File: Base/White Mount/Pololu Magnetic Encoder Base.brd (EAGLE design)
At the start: 26.7 x 33.7 mm, 0 parts

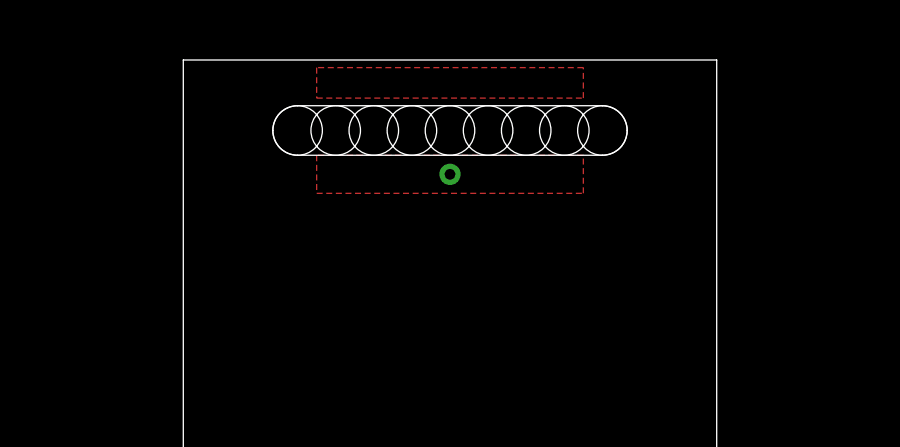
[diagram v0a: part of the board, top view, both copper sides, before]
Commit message: Added drill holes in slot
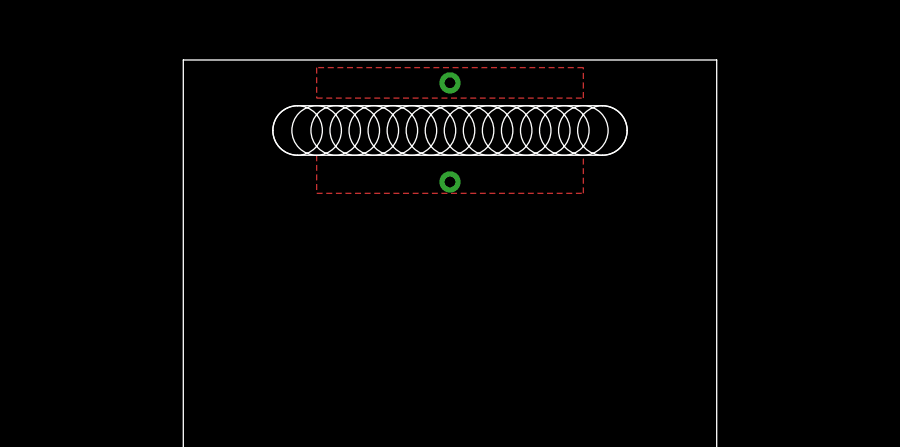
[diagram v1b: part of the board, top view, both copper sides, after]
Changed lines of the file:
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@@
 <text x="13.97" y="0.635" size="0.8128" layer="51" font="vector" ratio="12" align="bottom-center">AnomalousMaker.com</text>
 <hole x="8.89" y="31.3055" drill="1.651"/>
+<hole x="9.525" y="31.3055" drill="1.651"/>
 <hole x="10.16" y="31.3055" drill="1.651"/>
+<hole x="10.795" y="31.3055" drill="1.651"/>
 <hole x="11.43" y="31.3055" drill="1.651"/>
+<hole x="12.065" y="31.3055" drill="1.651"/>
 <hole x="12.7" y="31.3055" drill="1.651"/>
+<hole x="13.335" y="31.3055" drill="1.651"/>
 <hole x="13.97" y="31.3055" drill="1.651"/>
+<hole x="14.605" y="31.3055" drill="1.651"/>
 <hole x="15.24" y="31.3055" drill="1.651"/>
+<hole x="15.875" y="31.3055" drill="1.651"/>
 <hole x="16.51" y="31.3055" drill="1.651"/>
+<hole x="17.145" y="31.3055" drill="1.651"/>
 <hole x="17.78" y="31.3055" drill="1.651"/>
+<hole x="18.415" y="31.3055" drill="1.651"/>
 <hole x="19.05" y="31.3055" drill="1.651"/>
 </plain>
@@
 </class>
 </classes>
-<designrules name="default">
+<designrules name="OSHPark">
 <description language="de">&lt;b&gt;EAGLE Design Rules&lt;/b&gt;
 &lt;p&gt;
@@
 <param name="psElongationLong" value="100"/>
 <param name="psElongationOffset" value="100"/>
-<param name="mvStopFrame" value="1"/>
+<param name="mvStopFrame" value="0"/>
 <param name="mvCreamFrame" value="0"/>
-<param name="mlMinStopFrame" value="4mil"/>
-<param name="mlMaxStopFrame" value="4mil"/>
+<param name="mlMinStopFrame" value="0mil"/>
+<param name="mlMaxStopFrame" value="0mil"/>
 <param name="mlMinCreamFrame" value="0mil"/>
 <param name="mlMaxCreamFrame" value="0mil"/>
@@
 <vertex x="9.525" y="33.401"/>
 </polygon>
-</signal>
-<signal name="N$1">
-<via x="13.97" y="29.845" extent="1-16" drill="0.3556"/>
+<via x="13.97" y="29.591" extent="1-16" drill="0.3556"/>
+<via x="13.97" y="32.893" extent="1-16" drill="0.3556"/>
+<wire x1="13.97" y1="29.591" x2="13.97" y2="32.893" width="0" layer="19" extent="1-1"/>
 </signal>
 </signals>
